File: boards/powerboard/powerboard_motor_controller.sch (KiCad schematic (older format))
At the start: 34 parts, among them U301 LM3480-12, U302 DRV8332, U303 ACS711

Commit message: [powerboard] power supply
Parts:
- removed C302, C306, C311: 100n, Capacitors_SMD:C_0603, symbol C
- removed D303: Vishay LVB14A 13.2V, Diodes_SMD:D_SMB_Handsoldering, symbol D_Zener
- removed U301: LM3480-12, TO_SOT_Packages_SMD:SOT-23, symbol LM3480-12
- added U?: 7812SR-C, symbol LM7812
- C301: value 4µ7 -> 4µ7 0805
- C303: value 1µ -> 10µ
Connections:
- net labels added: +12V
- wire segments 127 -> 119
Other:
- moved on the sheet: C312
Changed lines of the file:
@@
-	1    0    0    -1
-$EndComp
-$Comp
-L LM3480-12 U301
-U 1 1 5939D01D
-P 2750 6350
-F 0 "U301" H 2450 6500 50  0000 L CNN
-F 1 "LM3480-12" H 3050 6500 50  0000 R CNN
-F 2 "TO_SOT_Packages_SMD:SOT-23" H 2750 5950 50  0001 C CIN
-F 3 "" H 2750 6350 50  0001 C CNN
-	1    2750 6350
 	1    0    0    -1
 $EndComp
@@
 Text Label 1050 6350 0    60   ~ 0
 V_IN
-$Comp
-L C C302
-U 1 1 5939DE85
-P 2000 6600
-F 0 "C302" H 2025 6700 50  0000 L CNN
-F 1 "100n" H 2025 6500 50  0000 L CNN
-F 2 "Capacitors_SMD:C_0603" H 2038 6450 50  0001 C CNN
-F 3 "" H 2000 6600 50  0001 C CNN
-	1    2000 6600
-	1    0    0    -1
-$EndComp
 $Comp
 L GND #PWR049
@@
 P 3350 6600
 F 0 "C303" H 3375 6700 50  0000 L CNN
-F 1 "1µ" H 3375 6500 50  0000 L CNN
+F 1 "10µ" H 3375 6500 50  0000 L CNN
 F 2 "Capacitors_SMD:C_0603" H 3388 6450 50  0001 C CNN
 F 3 "" H 3350 6600 50  0001 C CNN
@@
 P 1550 6600
 F 0 "C301" H 1575 6700 50  0000 L CNN
-F 1 "4µ7" H 1575 6500 50  0000 L CNN
+F 1 "4µ7 0805" H 1575 6500 50  0000 L CNN
 F 2 "Capacitors_SMD:C_0603" H 1588 6450 50  0001 C CNN
 F 3 "" H 1550 6600 50  0001 C CNN
@@
 	1    0    0    -1
 $EndComp
-Text Label 4600 6350 2    60   ~ 0
-12V
 Text Label 2700 3750 0    60   ~ 0
 12V
@@
 	1    0    0    -1
 $EndComp
-Text Label 5200 2650 2    60   ~ 0
-12V
 Wire Wire Line
 	3300 3200 3400 3200
@@
 Connection ~ 5650 1800
 Wire Wire Line
-	2250 6350 1050 6350
+	1050 6350 2350 6350
 Wire Wire Line
 	2750 6650 2750 6950
 Wire Wire Line
 	1550 6850 4600 6850
-Wire Wire Line
-	2000 6850 2000 6750
 Connection ~ 2750 6850
 Wire Wire Line
 	1550 6850 1550 6750
-Connection ~ 2000 6850
 Wire Wire Line
 	1550 6450 1550 6350
 Connection ~ 1550 6350
 Wire Wire Line
-	2000 6450 2000 6350
-Connection ~ 2000 6350
-Wire Wire Line
 	3350 6850 3350 6750
 Wire Wire Line
-	3250 6350 5000 6350
+	3150 6350 5000 6350
 Wire Wire Line
 	3350 6350 3350 6450
@@
 	6300 2850 6300 2300
 Wire Wire Line
-	5200 2650 4950 2650
+	4950 2650 5450 2650
 Wire Wire Line
 	4950 2950 5050 2950
@@
 Connection ~ 6000 1800
 $Comp
-L C C306
-U 1 1 5939B19F
-P 3700 6600
-F 0 "C306" H 3725 6700 50  0000 L CNN
-F 1 "100n" H 3725 6500 50  0000 L CNN
-F 2 "Capacitors_SMD:C_0603" H 3738 6450 50  0001 C CNN
-F 3 "" H 3700 6600 50  0001 C CNN
-	1    3700 6600
-	1    0    0    -1
-$EndComp
-$Comp
-L C C311
-U 1 1 5939B213
-P 3950 6600
-F 0 "C311" H 3975 6700 50  0000 L CNN
-F 1 "100n" H 3975 6500 50  0000 L CNN
-F 2 "Capacitors_SMD:C_0603" H 3988 6450 50  0001 C CNN
-F 3 "" H 3950 6600 50  0001 C CNN
-	1    3950 6600
-	1    0    0    -1
-$EndComp
-$Comp
 L C C312
 U 1 1 5939B286
-P 4200 6600
-F 0 "C312" H 4225 6700 50  0000 L CNN
-F 1 "100n" H 4225 6500 50  0000 L CNN
-F 2 "Capacitors_SMD:C_0603" H 4238 6450 50  0001 C CNN
-F 3 "" H 4200 6600 50  0001 C CNN
-	1    4200 6600
-	1    0    0    -1
-$EndComp
-Wire Wire Line
-	3700 6850 3700 6750
-Connection ~ 3350 6850
-Wire Wire Line
-	3950 6850 3950 6750
-Connection ~ 3700 6850
-Wire Wire Line
-	4200 6850 4200 6750
-Connection ~ 3950 6850
-Wire Wire Line
-	4200 6450 4200 6350
-Connection ~ 4200 6350
-Wire Wire Line
-	3950 6450 3950 6350
-Connection ~ 3950 6350
-Wire Wire Line
-	3700 6450 3700 6350
-Connection ~ 3700 6350
-$Comp
-L D_Zener D303
-U 1 1 5939BD90
 P 4600 6600
-F 0 "D303" H 4600 6700 50  0000 C CNN
-F 1 "Vishay LVB14A 13.2V" V 4900 6600 50  0000 C CNN
-F 2 "Diodes_SMD:D_SMB_Handsoldering" H 4600 6600 50  0001 C CNN
+F 0 "C312" H 4625 6700 50  0000 L CNN
+F 1 "100n" H 4625 6500 50  0000 L CNN
+F 2 "Capacitors_SMD:C_0603" H 4638 6450 50  0001 C CNN
 F 3 "" H 4600 6600 50  0001 C CNN
 	1    4600 6600
-	0    1    1    0
-$EndComp
-Wire Wire Line
-	4600 6850 4600 6750
-Connection ~ 4200 6850
-Wire Wire Line
-	4600 6350 4600 6450
-Connection ~ 4600 6350
+	1    0    0    -1
+$EndComp
+Connection ~ 3350 6850
 $Comp
 L C C319
@@
 Wire Wire Line
 	7050 4800 7050 4900
+$Comp
+L LM7812 U?
+U 1 1 5A192C4C
+P 2750 6400
+F 0 "U?" H 2900 6204 50  0000 C CNN
+F 1 "7812SR-C" H 2750 6600 50  0000 C CNN
+F 2 "" H 2750 6400 50  0001 C CNN
+F 3 "" H 2750 6400 50  0001 C CNN
+	1    2750 6400
+	1    0    0    -1
+$EndComp
+$Comp
+L +12V #PWR?
+U 1 1 5A194A5C
+P 5000 6350
+F 0 "#PWR?" H 5000 6200 50  0001 C CNN
+F 1 "+12V" H 5000 6490 50  0000 C CNN
+F 2 "" H 5000 6350 50  0001 C CNN
+F 3 "" H 5000 6350 50  0001 C CNN
+	1    5000 6350
+	0    1    1    0
+$EndComp
+$Comp
+L +12V #PWR?
+U 1 1 5A194AD4
+P 5450 2650
+F 0 "#PWR?" H 5450 2500 50  0001 C CNN
+F 1 "+12V" H 5450 2790 50  0000 C CNN
+F 2 "" H 5450 2650 50  0001 C CNN
+F 3 "" H 5450 2650 50  0001 C CNN
+	1    5450 2650
+	0    1    1    0
+$EndComp
+Wire Wire Line
+	4600 6850 4600 6750
+Wire Wire Line
+	4600 6450 4600 6350
+Connection ~ 4600 6350
 $EndSCHEMATC

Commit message: [powerboard] fix minor issues in all schematics; revision: rev10
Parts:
- C301: footprint Capacitors_SMD:C_0603 -> Capacitors_SMD:C_0805
- C307: value 4µ7 -> 1µ
- C313: value 47µ -> 4µ7 0805
- D304, D305, D306: footprint Diodes_SMD:D_SMB_Handsoldering -> Diodes_SMD:D_SMB_Standard
- R303: value 150k -> 200k
- U301: renamed from U?; footprint (none) -> TO_SOT_Packages_THT:TO-220_Vertical
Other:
- note added: "1.4A current limit"
- note removed: "1.9A current limit"
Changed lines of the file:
@@
 Sheet 3 11
 Title "Powerboard motor controller"
-Date "2017-03-14"
-Rev "20"
+Date "2017-11-23"
+Rev "rev10"
 Comp "VIPER"
 Comment1 ""
@@
 P 3150 3600
 F 0 "R303" V 3230 3600 50  0000 C CNN
-F 1 "150k" V 3150 3600 50  0000 C CNN
+F 1 "200k" V 3150 3600 50  0000 C CNN
 F 2 "Resistors_SMD:R_0603" V 3080 3600 50  0001 C CNN
 F 3 "" H 3150 3600 50  0001 C CNN
@@
 VREG
 Text Notes 1850 3750 0    60   ~ 0
-1.9A current limit
+1.4A current limit
 $Comp
 L GND #PWR048
@@
 P 5750 1600
 F 0 "C307" H 5775 1700 50  0000 L CNN
-F 1 "4µ7" H 5775 1500 50  0000 L CNN
+F 1 "1µ" H 5775 1500 50  0000 L CNN
 F 2 "Capacitors_SMD:C_0603" H 5788 1450 50  0001 C CNN
 F 3 "" H 5750 1600 50  0001 C CNN
@@
 F 0 "C301" H 1575 6700 50  0000 L CNN
 F 1 "4µ7 0805" H 1575 6500 50  0000 L CNN
-F 2 "Capacitors_SMD:C_0603" H 1588 6450 50  0001 C CNN
+F 2 "Capacitors_SMD:C_0805" H 1588 6450 50  0001 C CNN
 F 3 "" H 1550 6600 50  0001 C CNN
 	1    1550 6600
@@
 F 0 "D304" H 7350 2850 50  0000 C CNN
 F 1 "SMBJ40CA" H 7350 2650 50  0000 C CNN
-F 2 "Diodes_SMD:D_SMB_Handsoldering" H 7350 2750 50  0001 C CNN
+F 2 "Diodes_SMD:D_SMB_Standard" H 7350 2750 50  0001 C CNN
 F 3 "" H 7350 2750 50  0001 C CNN
 	1    7350 2750
@@
 F 0 "D305" H 7700 2850 50  0000 C CNN
 F 1 "SMBJ40CA" H 7700 2650 50  0000 C CNN
-F 2 "Diodes_SMD:D_SMB_Handsoldering" H 7700 2750 50  0001 C CNN
+F 2 "Diodes_SMD:D_SMB_Standard" H 7700 2750 50  0001 C CNN
 F 3 "" H 7700 2750 50  0001 C CNN
 	1    7700 2750
@@
 F 0 "D306" H 8050 2850 50  0000 C CNN
 F 1 "SMBJ40CA" H 8050 2650 50  0000 C CNN
-F 2 "Diodes_SMD:D_SMB_Handsoldering" H 8050 2750 50  0001 C CNN
+F 2 "Diodes_SMD:D_SMB_Standard" H 8050 2750 50  0001 C CNN
 F 3 "" H 8050 2750 50  0001 C CNN
 	1    8050 2750
@@
 P 5500 1600
 F 0 "C313" H 5525 1700 50  0000 L CNN
-F 1 "47µ" H 5525 1500 50  0000 L CNN
+F 1 "4µ7 0805" V 5450 1150 50  0000 L CNN
 F 2 "Capacitors_SMD:C_0603" H 5538 1450 50  0001 C CNN
 F 3 "" H 5500 1600 50  0001 C CNN
@@
 	7050 4800 7050 4900
 $Comp
-L LM7812 U?
+L LM7812 U301
 U 1 1 5A192C4C
 P 2750 6400
-F 0 "U?" H 2900 6204 50  0000 C CNN
+F 0 "U301" H 2900 6204 50  0000 C CNN
 F 1 "7812SR-C" H 2750 6600 50  0000 C CNN
-F 2 "" H 2750 6400 50  0001 C CNN
+F 2 "TO_SOT_Packages_THT:TO-220_Vertical" H 2750 6400 50  0001 C CNN
 F 3 "" H 2750 6400 50  0001 C CNN
 	1    2750 6400
@@
 $EndComp
 $Comp
-L +12V #PWR?
+L +12V #PWR052
 U 1 1 5A194A5C
 P 5000 6350
-F 0 "#PWR?" H 5000 6200 50  0001 C CNN
+F 0 "#PWR052" H 5000 6200 50  0001 C CNN
 F 1 "+12V" H 5000 6490 50  0000 C CNN
 F 2 "" H 5000 6350 50  0001 C CNN
@@
 $EndComp
 $Comp
-L +12V #PWR?
+L +12V #PWR053
 U 1 1 5A194AD4
 P 5450 2650
-F 0 "#PWR?" H 5450 2500 50  0001 C CNN
+F 0 "#PWR053" H 5450 2500 50  0001 C CNN
 F 1 "+12V" H 5450 2790 50  0000 C CNN
 F 2 "" H 5450 2650 50  0001 C CNN

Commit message: [powerboard] fix some footprint assignments
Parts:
- removed U301: 7812SR-C, TO_SOT_Packages_THT:TO-220_Vertical, symbol LM7812
- added U301: 7812SR-C, TO_SOT_Packages_THT:TO-220_Vertical, symbol LM7812CT
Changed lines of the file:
@@
 	7050 4800 7050 4900
-$Comp
-L LM7812 U301
-U 1 1 5A192C4C
-P 2750 6400
-F 0 "U301" H 2900 6204 50  0000 C CNN
-F 1 "7812SR-C" H 2750 6600 50  0000 C CNN
-F 2 "TO_SOT_Packages_THT:TO-220_Vertical" H 2750 6400 50  0001 C CNN
-F 3 "" H 2750 6400 50  0001 C CNN
-	1    2750 6400
-	1    0    0    -1
-$EndComp
 $Comp
 L +12V #PWR052
@@
 	4600 6450 4600 6350
 Connection ~ 4600 6350
+$Comp
+L LM7812CT U301
+U 1 1 5A1DB61B
+P 2750 6400
+F 0 "U301" H 2550 6600 50  0000 C CNN
+F 1 "7812SR-C" H 2750 6600 50  0000 L CNN
+F 2 "TO_SOT_Packages_THT:TO-220_Vertical" H 2750 6500 50  0001 C CIN
+F 3 "" H 2750 6400 50  0001 C CNN
+	1    2750 6400
+	1    0    0    -1
+$EndComp
 $EndSCHEMATC

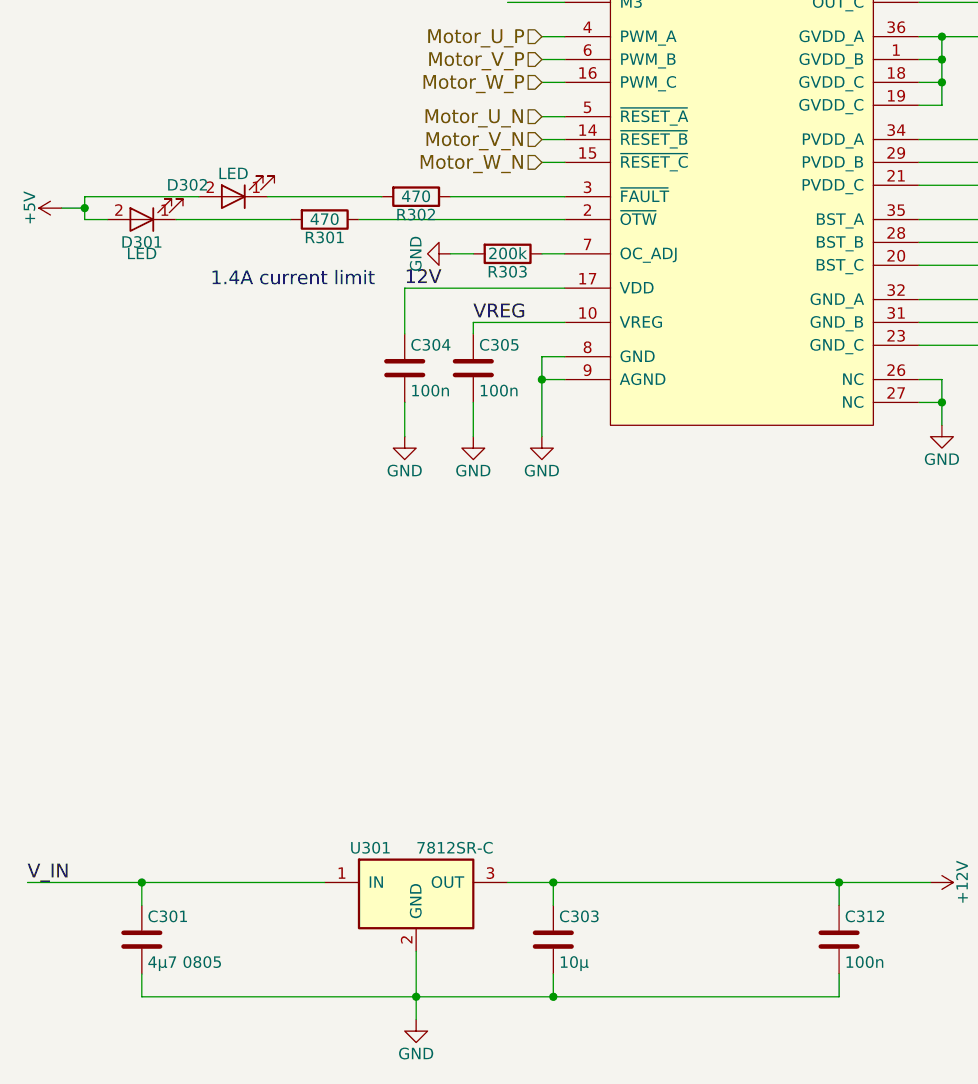
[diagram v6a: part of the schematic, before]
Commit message: [powerboard] layout rev10; some changes to the schematic
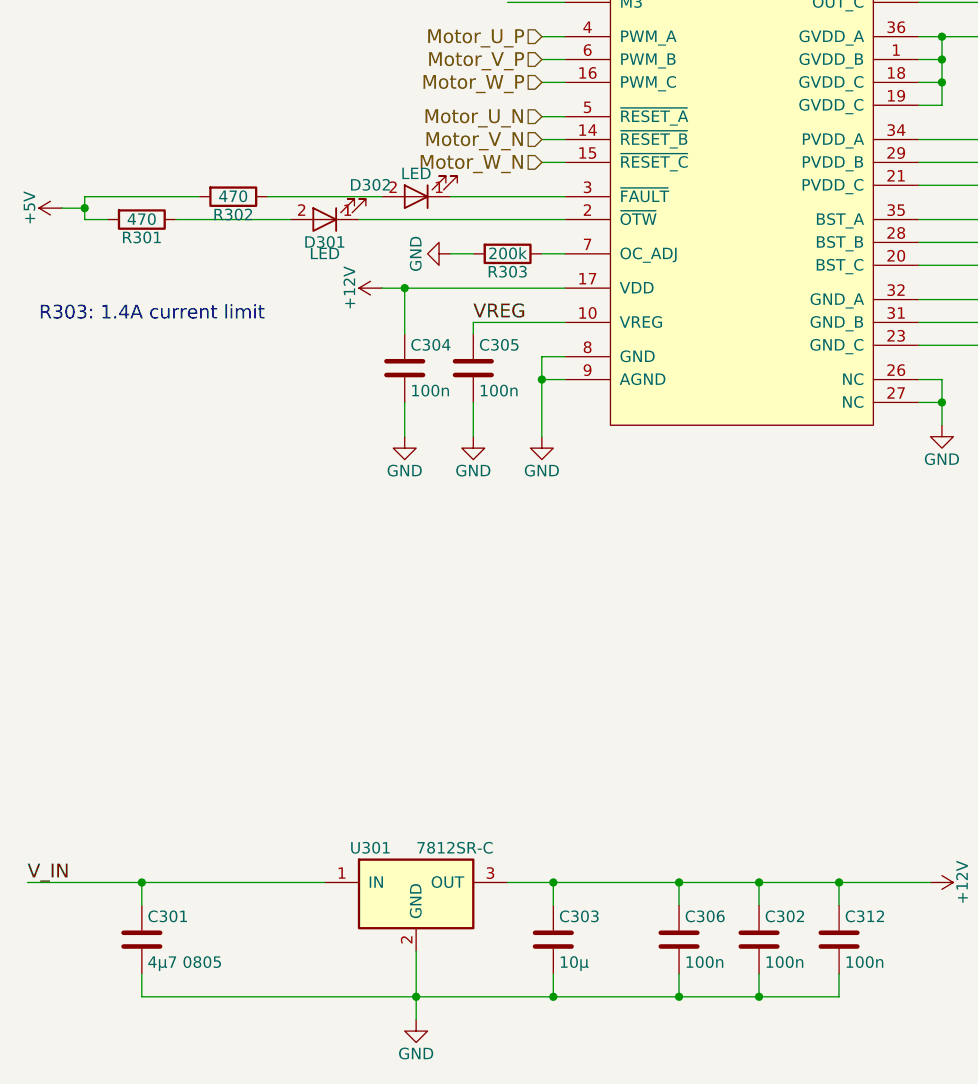
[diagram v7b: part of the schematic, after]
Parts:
- added C302, C306: 100n, Capacitors_SMD:C_0603, symbol C
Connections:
- net 12V is gone; now on net +12V: C304.1, U302.17 (VDD)
- net +12V: now also C302.1, C306.1
- net +5V: now also R301.2, R302.2; no longer D301.2 (A), D302.2 (A)
- net GND: now also C302.2, C306.2
- net at D302.1 (K): now also U302.3 (~FAULT); no longer R302.2
- net at D301.1 (K): now also U302.2 (~OTW); no longer R301.2
- net at R302.1: now also D302.2 (A); no longer U302.3 (~FAULT)
- net at R301.1: now also D301.2 (A); no longer U302.2 (~OTW)
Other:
- note added: "R303: 1.4A current limit"
- note removed: "1.4A current limit"
- moved on the sheet: D301, D302, R301, R302
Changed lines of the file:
@@
 L LED D302
 U 1 1 59379B27
-P 1950 3350
-F 0 "D302" H 2150 3300 50  0000 C CNN
-F 1 "LED" H 1950 3250 50  0000 C CNN
-F 2 "LEDs:LED_0603" H 1950 3350 50  0001 C CNN
-F 3 "" H 1950 3350 50  0001 C CNN
-	1    1950 3350
+P 2750 3350
+F 0 "D302" H 2950 3300 50  0000 C CNN
+F 1 "LED" H 2750 3250 50  0000 C CNN
+F 2 "LEDs:LED_0603" H 2750 3350 50  0001 C CNN
+F 3 "" H 2750 3350 50  0001 C CNN
+	1    2750 3350
 	-1   0    0    1
 $EndComp
@@
 L LED D301
 U 1 1 59379B92
-P 1550 3450
-F 0 "D301" H 1550 3550 50  0000 C CNN
-F 1 "LED" H 1550 3600 50  0000 C CNN
-F 2 "LEDs:LED_0603" H 1550 3450 50  0001 C CNN
-F 3 "" H 1550 3450 50  0001 C CNN
-	1    1550 3450
+P 2350 3450
+F 0 "D301" H 2350 3550 50  0000 C CNN
+F 1 "LED" H 2350 3600 50  0000 C CNN
+F 2 "LEDs:LED_0603" H 2350 3450 50  0001 C CNN
+F 3 "" H 2350 3450 50  0001 C CNN
+	1    2350 3450
 	-1   0    0    1
 $EndComp
 $Comp
-L +5V #PWR039
+L +5V #PWR042
 U 1 1 59379BBE
 P 1200 3400
-F 0 "#PWR039" H 1200 3250 50  0001 C CNN
+F 0 "#PWR042" H 1200 3250 50  0001 C CNN
 F 1 "+5V" H 1200 3540 50  0000 C CNN
 F 2 "" H 1200 3400 50  0001 C CNN
@@
 L R R302
 U 1 1 59379C3A
-P 2750 3350
-F 0 "R302" V 2830 3350 50  0000 C CNN
-F 1 "470" V 2750 3350 50  0000 C CNN
-F 2 "Resistors_SMD:R_0603" V 2680 3350 50  0001 C CNN
-F 3 "" H 2750 3350 50  0001 C CNN
-	1    2750 3350
+P 1950 3350
+F 0 "R302" V 2030 3350 50  0000 C CNN
+F 1 "470" V 1950 3350 50  0000 C CNN
+F 2 "Resistors_SMD:R_0603" V 1880 3350 50  0001 C CNN
+F 3 "" H 1950 3350 50  0001 C CNN
+	1    1950 3350
 	0    1    1    0
 $EndComp
@@
 L R R301
 U 1 1 59379C8A
-P 2350 3450
-F 0 "R301" V 2430 3450 50  0000 C CNN
-F 1 "470" V 2350 3450 50  0000 C CNN
-F 2 "Resistors_SMD:R_0603" V 2280 3450 50  0001 C CNN
-F 3 "" H 2350 3450 50  0001 C CNN
-	1    2350 3450
+P 1550 3450
+F 0 "R301" V 1630 3450 50  0000 C CNN
+F 1 "470" V 1550 3450 50  0000 C CNN
+F 2 "Resistors_SMD:R_0603" V 1480 3450 50  0001 C CNN
+F 3 "" H 1550 3450 50  0001 C CNN
+	1    1550 3450
 	0    1    1    0
 $EndComp
 $Comp
-L GND #PWR040
+L GND #PWR043
 U 1 1 59379D87
 P 2900 3600
-F 0 "#PWR040" H 2900 3350 50  0001 C CNN
+F 0 "#PWR043" H 2900 3350 50  0001 C CNN
 F 1 "GND" H 2900 3450 50  0000 C CNN
 F 2 "" H 2900 3600 50  0001 C CNN
@@
 $EndComp
 $Comp
-L GND #PWR041
+L GND #PWR044
 U 1 1 5937A00C
 P 5600 5000
-F 0 "#PWR041" H 5600 4750 50  0001 C CNN
+F 0 "#PWR044" H 5600 4750 50  0001 C CNN
 F 1 "GND" H 5600 4850 50  0000 C CNN
 F 2 "" H 5600 5000 50  0001 C CNN
@@
 $EndComp
 $Comp
-L GND #PWR042
+L GND #PWR045
 U 1 1 5937A030
 P 3300 4400
-F 0 "#PWR042" H 3300 4150 50  0001 C CNN
+F 0 "#PWR045" H 3300 4150 50  0001 C CNN
 F 1 "GND" H 3300 4250 50  0000 C CNN
 F 2 "" H 3300 4400 50  0001 C CNN
@@
 $EndComp
 $Comp
-L +3V3 #PWR043
+L +3V3 #PWR046
 U 1 1 5937A989
 P 6800 4500
-F 0 "#PWR043" H 6800 4350 50  0001 C CNN
+F 0 "#PWR046" H 6800 4350 50  0001 C CNN
 F 1 "+3V3" H 6800 4640 50  0000 C CNN
 F 2 "" H 6800 4500 50  0001 C CNN
@@
 $EndComp
 $Comp
-L GND #PWR044
+L GND #PWR047
 U 1 1 5937A9B1
 P 6800 5000
-F 0 "#PWR044" H 6800 4750 50  0001 C CNN
+F 0 "#PWR047" H 6800 4750 50  0001 C CNN
 F 1 "GND" H 6800 4850 50  0000 C CNN
 F 2 "" H 6800 5000 50  0001 C CNN
@@
 Current
 $Comp
-L GND #PWR045
+L GND #PWR048
 U 1 1 5938B958
 P 3300 2200
-F 0 "#PWR045" H 3300 1950 50  0001 C CNN
+F 0 "#PWR048" H 3300 1950 50  0001 C CNN
 F 1 "GND" H 3300 2050 50  0000 C CNN
 F 2 "" H 3300 2200 50  0001 C CNN
@@
 $EndComp
 $Comp
-L GND #PWR046
+L GND #PWR049
 U 1 1 5938C0D3
 P 3000 4400
-F 0 "#PWR046" H 3000 4150 50  0001 C CNN
+F 0 "#PWR049" H 3000 4150 50  0001 C CNN
 F 1 "GND" H 3000 4250 50  0000 C CNN
 F 2 "" H 3000 4400 50  0001 C CNN
@@
 $EndComp
 $Comp
-L GND #PWR047
+L GND #PWR050
 U 1 1 5938C102
 P 2700 4400
-F 0 "#PWR047" H 2700 4150 50  0001 C CNN
+F 0 "#PWR050" H 2700 4150 50  0001 C CNN
 F 1 "GND" H 2700 4250 50  0000 C CNN
 F 2 "" H 2700 4400 50  0001 C CNN
@@
 Text Label 3150 2500 0    60   ~ 0
 VREG
-Text Notes 1850 3750 0    60   ~ 0
-1.4A current limit
-$Comp
-L GND #PWR048
+Text Notes 1100 3900 0    60   ~ 0
+R303: 1.4A current limit
+$Comp
+L GND #PWR051
 U 1 1 5939C50C
 P 5650 1850
-F 0 "#PWR048" H 5650 1600 50  0001 C CNN
+F 0 "#PWR051" H 5650 1600 50  0001 C CNN
 F 1 "GND" H 5650 1700 50  0000 C CNN
 F 2 "" H 5650 1850 50  0001 C CNN
@@
 V_IN
 $Comp
-L GND #PWR049
+L GND #PWR052
 U 1 1 5939E00D
 P 2750 6950
-F 0 "#PWR049" H 2750 6700 50  0001 C CNN
+F 0 "#PWR052" H 2750 6700 50  0001 C CNN
 F 1 "GND" H 2750 6800 50  0000 C CNN
 F 2 "" H 2750 6950 50  0001 C CNN
@@
 	1    0    0    -1
 $EndComp
-Text Label 2700 3750 0    60   ~ 0
-12V
 $Comp
 L DRV8332 U302
@@
 Connection ~ 3300 2300
 Wire Wire Line
-	3400 3750 2700 3750
+	2600 3750 3400 3750
 Wire Wire Line
 	2700 3750 2700 3950
@@
 Connection ~ 5250 4000
 $Comp
-L GND #PWR050
+L GND #PWR053
 U 1 1 59385450
 P 5050 4350
-F 0 "#PWR050" H 5050 4100 50  0001 C CNN
+F 0 "#PWR053" H 5050 4100 50  0001 C CNN
 F 1 "GND" H 5050 4200 50  0000 C CNN
 F 2 "" H 5050 4350 50  0001 C CNN
@@
 $EndComp
 $Comp
-L GND #PWR051
+L GND #PWR054
 U 1 1 59453906
 P 7050 5300
-F 0 "#PWR051" H 7050 5050 50  0001 C CNN
+F 0 "#PWR054" H 7050 5050 50  0001 C CNN
 F 1 "GND" H 7050 5150 50  0000 C CNN
 F 2 "" H 7050 5300 50  0001 C CNN
@@
 	7050 4800 7050 4900
 $Comp
-L +12V #PWR052
+L +12V #PWR055
 U 1 1 5A194A5C
 P 5000 6350
-F 0 "#PWR052" H 5000 6200 50  0001 C CNN
+F 0 "#PWR055" H 5000 6200 50  0001 C CNN
 F 1 "+12V" H 5000 6490 50  0000 C CNN
 F 2 "" H 5000 6350 50  0001 C CNN
@@
 $EndComp
 $Comp
-L +12V #PWR053
+L +12V #PWR056
 U 1 1 5A194AD4
 P 5450 2650
-F 0 "#PWR053" H 5450 2500 50  0001 C CNN
+F 0 "#PWR056" H 5450 2500 50  0001 C CNN
 F 1 "+12V" H 5450 2790 50  0000 C CNN
 F 2 "" H 5450 2650 50  0001 C CNN
@@
 	1    0    0    -1
 $EndComp
+$Comp
+L +12V #PWR057
+U 1 1 5A1B25BF
+P 2600 3750
+F 0 "#PWR057" H 2600 3600 50  0001 C CNN
+F 1 "+12V" H 2600 3890 50  0000 C CNN
+F 2 "" H 2600 3750 50  0001 C CNN
+F 3 "" H 2600 3750 50  0001 C CNN
+	1    2600 3750
+	0    -1   -1   0
+$EndComp
+Connection ~ 2700 3750
+$Comp
+L C C302
+U 1 1 5A1B517D
+P 4250 6600
+F 0 "C302" H 4275 6700 50  0000 L CNN
+F 1 "100n" H 4275 6500 50  0000 L CNN
+F 2 "Capacitors_SMD:C_0603" H 4288 6450 50  0001 C CNN
+F 3 "" H 4250 6600 50  0001 C CNN
+	1    4250 6600
+	1    0    0    -1
+$EndComp
+Wire Wire Line
+	4250 6450 4250 6350
+Connection ~ 4250 6350
+Wire Wire Line
+	4250 6750 4250 6850
+Connection ~ 4250 6850
+$Comp
+L C C306
+U 1 1 5A1B58BC
+P 3900 6600
+F 0 "C306" H 3925 6700 50  0000 L CNN
+F 1 "100n" H 3925 6500 50  0000 L CNN
+F 2 "Capacitors_SMD:C_0603" H 3938 6450 50  0001 C CNN
+F 3 "" H 3900 6600 50  0001 C CNN
+	1    3900 6600
+	1    0    0    -1
+$EndComp
+Wire Wire Line
+	3900 6450 3900 6350
+Connection ~ 3900 6350
+Wire Wire Line
+	3900 6750 3900 6850
+Connection ~ 3900 6850
 $EndSCHEMATC

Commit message: [board][powerboard] Update Board to rev11
* Increase distance between 12V-Regulator and Mounting Hole
* Add TVS diode SMAJ36A to 12V regulator input
* Populate C120 (50SVPK68M)
* Add RC-filter to Hall-Sensor lines
  * f_g = 7kHz (470 ohms, 22nF)
* End Switch Pull-Down
* Hall-Sensor Pull-Up
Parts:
- C301, C302, C303, C304, C305, C306, C307, C308, C309, C310, C312, C313, C314, C315, C316, C317, C318, C319: symbol C -> powerboard-rescue:C
- D301, D302: symbol LED -> powerboard-rescue:LED
- D304, D305, D306: symbol D_TVS -> powerboard-rescue:D_TVS
- L301, L302, L303: symbol L_Small -> powerboard-rescue:L_Small
- R301, R302, R303: symbol R -> powerboard-rescue:R
- U301: symbol LM7812CT -> powerboard-rescue:LM7812CT
- U302: symbol DRV8332 -> drv8332:DRV8332
- U303: symbol ACS711 -> ACS711:ACS711
